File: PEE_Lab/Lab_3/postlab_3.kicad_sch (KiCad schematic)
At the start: 7 parts, among them U1 LM741

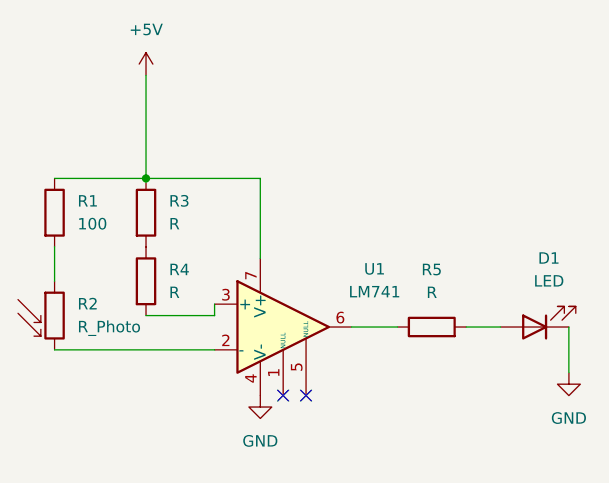
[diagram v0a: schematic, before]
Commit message: Rearrange resistors into correct positions
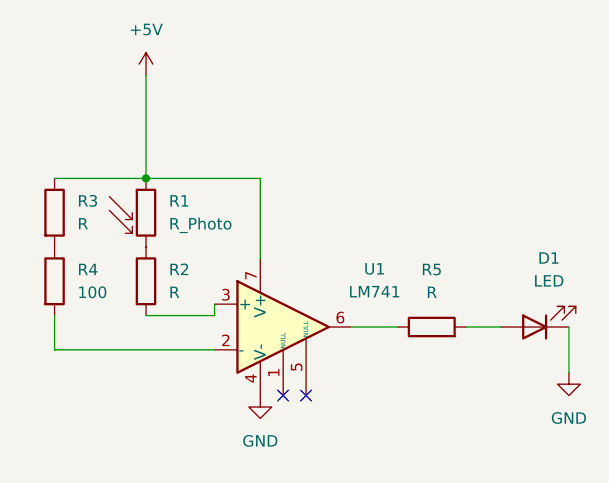
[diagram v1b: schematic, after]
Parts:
- renumbered R2 to R1, R4 to R2, R1 to R4
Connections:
- net +5V: now also R1.1; no longer R4.1
- net at U1.2 (-): now also R4.2; no longer R1.2
- net at R2.1: now also R1.2; no longer R3.2
- new net: R3.2, R4.1
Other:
- moved on the sheet: R1, R3, R4
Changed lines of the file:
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@@
+	(wire
+		(pts
+			(xy 55.88 88.9) (xy 55.88 92.71)
+		)
+		(stroke
+			(width 0)
+			(type default)
+		)
+	)
 	(wire
 		(pts
@@
 	(wire
 		(pts
+			(xy 66.04 88.9) (xy 73.66 88.9)
+		)
+		(stroke
+			(width 0)
+			(type default)
+		)
+	)
+	(wire
+		(pts
 			(xy 55.88 92.71) (xy 73.66 92.71)
 		)
@@
 	(wire
 		(pts
-			(xy 66.04 88.9) (xy 73.66 88.9)
-		)
-		(stroke
-			(width 0)
-			(type default)
-		)
-	)
-	(wire
-		(pts
 			(xy 73.66 88.9) (xy 73.66 87.63)
 		)
@@
 		(pts
 			(xy 66.04 62.23) (xy 66.04 73.66)
-		)
-		(stroke
-			(width 0)
-			(type default)
-		)
-	)
-	(wire
-		(pts
-			(xy 55.88 85.09) (xy 55.88 81.28)
 		)
 		(stroke
@@
 	(symbol
 		(lib_id "Device:R_Photo")
-		(at 55.88 88.9 0)
-		(unit 1)
-		(exclude_from_sim no)
-		(in_bom yes)
-		(on_board yes)
-		(dnp no)
-		(fields_autoplaced yes)
-		(property "Reference" "R2"
-			(at 58.42 87.6299 0)
+		(at 66.04 77.47 0)
+		(unit 1)
+		(exclude_from_sim no)
+		(in_bom yes)
+		(on_board yes)
+		(dnp no)
+		(fields_autoplaced yes)
+		(property "Reference" "R1"
+			(at 68.58 76.1999 0)
 			(effects
 				(font
@@
 		)
 		(property "Value" "R_Photo"
-			(at 58.42 90.1699 0)
-			(effects
-				(font
-					(size 1.27 1.27)
-				)
-				(justify left)
-			)
-		)
-		(property "Footprint" ""
-			(at 57.15 95.25 90)
+			(at 68.58 78.7399 0)
+			(effects
+				(font
+					(size 1.27 1.27)
+				)
+				(justify left)
+			)
+		)
+		(property "Footprint" ""
+			(at 67.31 83.82 90)
 			(effects
 				(font
@@
 		)
 		(property "Datasheet" "~"
-			(at 55.88 90.17 0)
+			(at 66.04 78.74 0)
 			(effects
 				(font
@@
 		)
 		(property "Description" "Photoresistor"
-			(at 55.88 88.9 0)
+			(at 66.04 77.47 0)
 			(effects
 				(font
@@
 			(project ""
 				(path "/5f26b856-fcba-4d0f-ae75-d4c6d9b6ff63"
-					(reference "R2")
+					(reference "R1")
 					(unit 1)
 				)
@@
 	(symbol
 		(lib_id "Device:R")
-		(at 66.04 77.47 0)
+		(at 55.88 77.47 0)
 		(unit 1)
 		(exclude_from_sim no)
@@
 		(fields_autoplaced yes)
 		(property "Reference" "R3"
-			(at 68.58 76.1999 0)
+			(at 58.42 76.1999 0)
 			(effects
 				(font
@@
 		)
 		(property "Value" "R"
-			(at 68.58 78.7399 0)
-			(effects
-				(font
-					(size 1.27 1.27)
-				)
-				(justify left)
-			)
-		)
-		(property "Footprint" ""
-			(at 64.262 77.47 90)
+			(at 58.42 78.7399 0)
+			(effects
+				(font
+					(size 1.27 1.27)
+				)
+				(justify left)
+			)
+		)
+		(property "Footprint" ""
+			(at 54.102 77.47 90)
 			(effects
 				(font
@@
 		)
 		(property "Datasheet" "~"
-			(at 66.04 77.47 0)
+			(at 55.88 77.47 0)
 			(effects
 				(font
@@
 		)
 		(property "Description" "Resistor"
-			(at 66.04 77.47 0)
+			(at 55.88 77.47 0)
 			(effects
 				(font
@@
 	(symbol
 		(lib_id "Device:R")
-		(at 55.88 77.47 0)
-		(unit 1)
-		(exclude_from_sim no)
-		(in_bom yes)
-		(on_board yes)
-		(dnp no)
-		(fields_autoplaced yes)
-		(property "Reference" "R1"
-			(at 58.42 76.1999 0)
+		(at 55.88 85.09 0)
+		(unit 1)
+		(exclude_from_sim no)
+		(in_bom yes)
+		(on_board yes)
+		(dnp no)
+		(fields_autoplaced yes)
+		(property "Reference" "R4"
+			(at 58.42 83.8199 0)
 			(effects
 				(font
@@
 		)
 		(property "Value" "100"
-			(at 58.42 78.7399 0)
-			(effects
-				(font
-					(size 1.27 1.27)
-				)
-				(justify left)
-			)
-		)
-		(property "Footprint" ""
-			(at 54.102 77.47 90)
+			(at 58.42 86.3599 0)
+			(effects
+				(font
+					(size 1.27 1.27)
+				)
+				(justify left)
+			)
+		)
+		(property "Footprint" ""
+			(at 54.102 85.09 90)
 			(effects
 				(font
@@
 		)
 		(property "Datasheet" "~"
-			(at 55.88 77.47 0)
+			(at 55.88 85.09 0)
 			(effects
 				(font
@@
 		)
 		(property "Description" "Resistor"
-			(at 55.88 77.47 0)
+			(at 55.88 85.09 0)
 			(effects
 				(font
@@
 			(project ""
 				(path "/5f26b856-fcba-4d0f-ae75-d4c6d9b6ff63"
-					(reference "R1")
+					(reference "R4")
 					(unit 1)
 				)
@@
 		(dnp no)
 		(fields_autoplaced yes)
-		(property "Reference" "R4"
+		(property "Reference" "R2"
 			(at 68.58 83.8199 0)
 			(effects
@@
 			(project "postlab_3"
 				(path "/5f26b856-fcba-4d0f-ae75-d4c6d9b6ff63"
-					(reference "R4")
-					(unit 1)
-				)
+					(reference "R2")
+					(unit 1)
+				)

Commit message: Implemented proper voltage divider in postlab 3
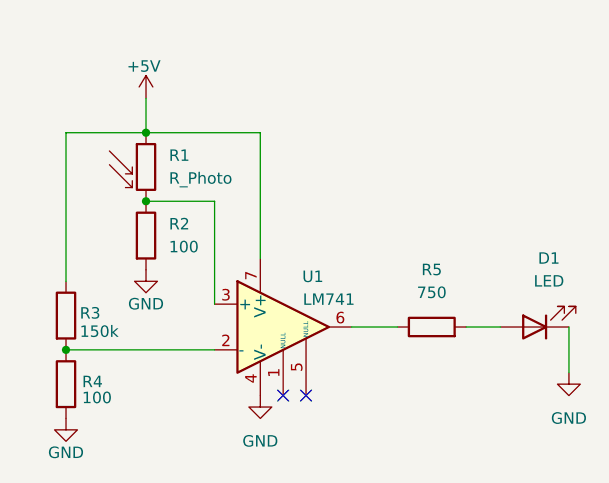
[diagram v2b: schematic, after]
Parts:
- R2: value R -> 100
- R3: value R -> 150k
- R5: value R -> 750
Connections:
- net GND: now also R2.2, R4.2
- net at U1.2 (-): now also R3.2, R4.1; no longer R4.2
- net at U1.3 (+): now also R1.2, R2.1; no longer R2.2
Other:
- moved on the sheet: R1, R2, R3, R4
